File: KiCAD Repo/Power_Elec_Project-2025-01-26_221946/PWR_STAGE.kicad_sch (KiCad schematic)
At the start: 0 parts

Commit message: PLF and GD circuit
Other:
- company: (none) -> M.Nguyen B.Patel S.Dupuis
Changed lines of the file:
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@@
 	(generator_version "8.0")
 	(paper "A4")
+	(title_block
+		(date "2025-02-21")
+		(rev "1")
+		(company "M.Nguyen B.Patel S.Dupuis")
+	)
 	(hierarchical_label "GND"
 		(shape input)

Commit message: PCB
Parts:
- added C15: 470uF, Capacitor_THT:CP_Radial_D10.0mm_P5.00mm, symbol Device:C
- added C16: 1uF, Capacitor_SMD:C_1206_3216Metric_Pad1.33x1.80mm_HandSolder, symbol Device:C
- added C17: 2.2uF, Capacitor_THT:CP_Radial_D8.0mm_P3.50mm, symbol Device:C
- added D6: SS310, Diode_SMD:D_SMA, symbol Diode:SS310
- added J1, J2, J3: RED, Connector:Banana_Jack_1Pin, symbol Connector:Conn_01x01_Pin
- added J4, J5: Black, Connector:Banana_Jack_1Pin, symbol Connector:Conn_01x01_Pin
- added L2: 2.2mH, Barrel Inductor AIRD-06-182K:AIRD-06_ABR, symbol Device:L
- added Q1: IRF540N, Package_TO_SOT_THT:TO-220-3_Vertical, symbol Transistor_FET:IRF540N
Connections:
- net VG: now also Q1.1 (G)
- net VOUT: now also C17.1, J3.1 (Pin_1), L2.2
- net VSW: now also D6.1 (K), J2.1 (Pin_1), L2.1, Q1.3 (S)
- new net: C15.2, C16.2, C17.2, D6.2 (A)
- new net GNDPWR: J4.1 (Pin_1), J5.1 (Pin_1)
- new net VDD: C15.1, C16.1, J1.1 (Pin_1), Q1.2 (D)
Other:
- note added: "Banana Jack"
- note added: "Internal IO"
- note added: "Power Stage"

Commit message: PCB
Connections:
- net GNDPWR: now also C15.2, C16.2, C17.2, D6.2 (A)
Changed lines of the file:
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@@
+	)
+	(junction
+		(at 144.78 114.3)
+		(diameter 0)
+		(color 0 0 0 0)
 	)
 	(junction
@@
 	(wire
 		(pts
+			(xy 144.78 114.3) (xy 149.86 114.3)
+		)
+		(stroke
+			(width 0)
+			(type default)
+		)
+	)
+	(wire
+		(pts
 			(xy 129.54 92.71) (xy 137.16 92.71)
 		)
@@
 	(wire
 		(pts
-			(xy 137.16 114.3) (xy 149.86 114.3)
+			(xy 137.16 114.3) (xy 144.78 114.3)
 		)
 		(stroke
@@
 	(rectangle
 		(start 120.65 85.09)
-		(end 210.82 118.11)
+		(end 210.82 120.65)
 		(stroke
 			(width 0)
@@
 					(unit 1)
 				)
+			)
+		)
+	)
+	(symbol
+		(lib_id "power:GNDPWR")
+		(at 144.78 114.3 0)
+		(unit 1)
+		(exclude_from_sim no)
+		(in_bom yes)
+		(on_board yes)
+		(dnp no)
+		(fields_autoplaced yes)
+		(property "Reference" "#PWR069"
+			(at 144.78 119.38 0)
+			(effects
+				(font
+					(size 1.27 1.27)
+				)
+				(hide yes)
+			)
+		)
+		(property "Value" "GNDPWR"
+			(at 144.653 118.11 0)
+			(effects
+				(font
+					(size 1.27 1.27)
+				)
+			)
+		)
+		(property "Footprint" ""
+			(at 144.78 115.57 0)
+			(effects
+				(font
+					(size 1.27 1.27)
+				)
+				(hide yes)
+			)
+		)
+		(property "Datasheet" ""
+			(at 144.78 115.57 0)
+			(effects
+				(font
+					(size 1.27 1.27)
+				)
+				(hide yes)
+			)
+		)
+		(property "Description" "Power symbol creates a global label with name \"GNDPWR\" , global ground"
+			(at 144.78 114.3 0)
+			(effects
+				(font
+					(size 1.27 1.27)
+				)
+				(hide yes)
+			)
+		)
+		(pin "1"
+		)
+		(instances
+			(project "Power_Elec_Project"
+				(path "/ecd51ed2-b30f-41c1-93fa-3d04786e684e/50dafc5c-3cd3-4388-aec3-9b121726b53c"
+					(reference "#PWR069")
+					(unit 1)
+				)

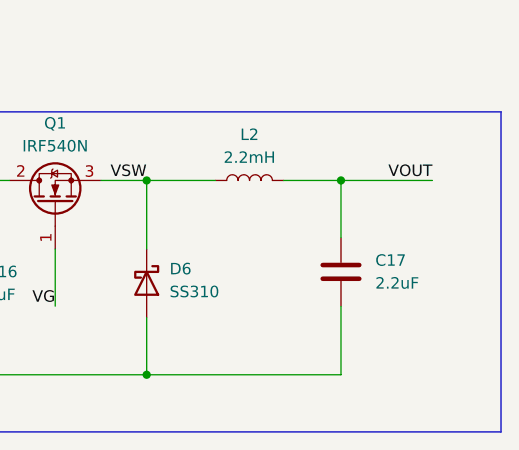
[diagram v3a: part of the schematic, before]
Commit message: Capacitor change
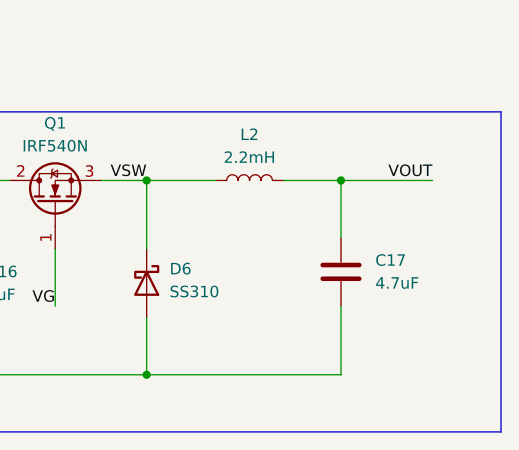
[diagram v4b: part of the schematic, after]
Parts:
- C17: value 2.2uF -> 4.7uF; footprint Capacitor_THT:CP_Radial_D8.0mm_P3.50mm -> Capacitor_SMD:C_1206_3216Metric_Pad1.33x1.80mm_HandSolder; Part Number A759KK225M2EAAE685 -> GRM319R61H475KA12D
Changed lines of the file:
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@@
 			)
 		)
-		(property "Value" "2.2uF"
+		(property "Value" "4.7uF"
 			(at 196.85 104.1399 0)
 			(effects
@@
 			)
 		)
-		(property "Footprint" "Capacitor_THT:CP_Radial_D8.0mm_P3.50mm"
+		(property "Footprint" "Capacitor_SMD:C_1206_3216Metric_Pad1.33x1.80mm_HandSolder"
 			(at 194.0052 106.68 0)
 			(effects
@@
 			)
 		)
-		(property "Description" "Unpolarized capacitor"
+		(property "Description" "4.7 µF ±10% 50V Ceramic Capacitor X5R 1206 (3216 Metric)"
 			(at 193.04 102.87 0)
 			(effects
@@
 			)
 		)
-		(property "Part Number" "A759KK225M2EAAE685"
+		(property "Part Number" "GRM319R61H475KA12D"
 			(at 193.04 102.87 0)
 			(effects

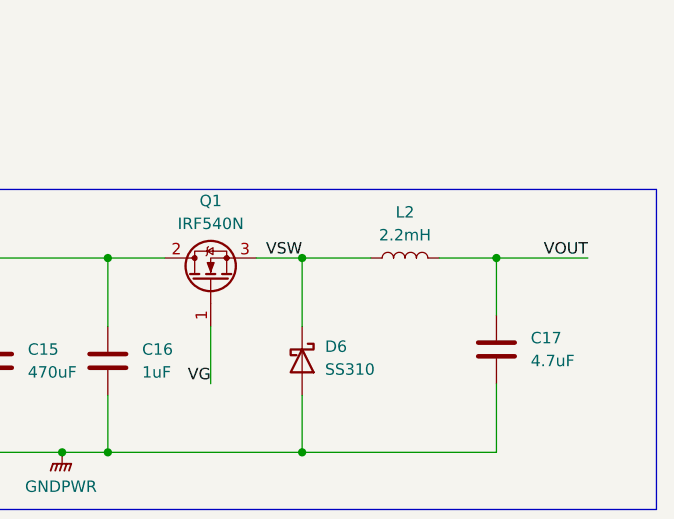
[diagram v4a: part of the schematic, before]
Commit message: Inductor and PCB fix
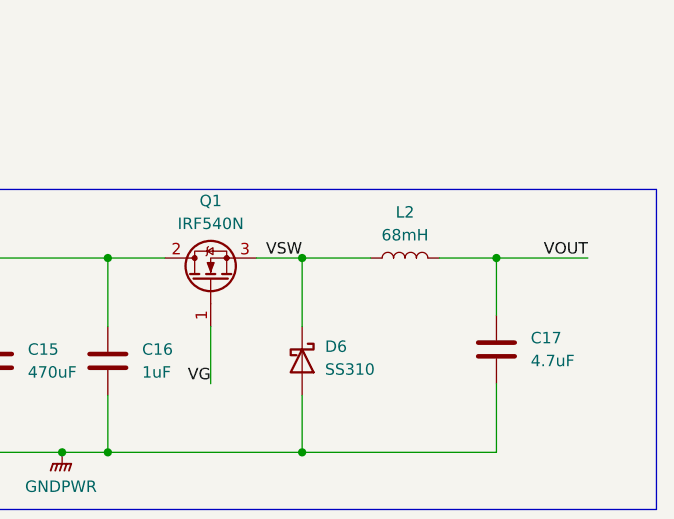
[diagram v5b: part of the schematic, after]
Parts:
- L2: value 2.2mH -> 68mH; footprint Barrel Inductor AIRD-06-182K:AIRD-06_ABR -> CustomLIB:Inductor_Throughhole_Radial; D=60mm, P=47mm; Part Number AIRD-06-182K -> RL-1256-7-68000
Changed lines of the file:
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@@
 			)
 		)
-		(property "Value" "2.2mH"
+		(property "Value" "68mH"
 			(at 182.88 90.17 90)
 			(effects
@@
 			)
 		)
-		(property "Footprint" "Barrel Inductor AIRD-06-182K:AIRD-06_ABR"
+		(property "Footprint" "CustomLIB:Inductor_Throughhole_Radial; D=60mm, P=47mm"
 			(at 182.88 92.71 0)
 			(effects
@@
 			)
 		)
-		(property "Description" "Inductor"
+		(property "Description" "68 mH Unshielded Wirewound Inductor 1.3 A 5.22Ohm Max Radial, Vertical Cylinder"
 			(at 182.88 92.71 0)
 			(effects
@@
 			)
 		)
-		(property "Part Number" "AIRD-06-182K"
+		(property "Part Number" "RL-1256-7-68000"
 			(at 182.88 92.71 0)
 			(effects
